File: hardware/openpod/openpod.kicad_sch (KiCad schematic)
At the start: 3 parts

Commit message: designed clickwheel and see if mpr121 can fit on it
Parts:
- ESP1: footprint openpod:ESP32-S3-WROOM-2 -> RF_Module:ESP32-S3-WROOM-2
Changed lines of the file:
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@@
       (effects (font (size 1.27 1.27)) (justify left))
     )
-    (property "Footprint" "openpod:ESP32-S3-WROOM-2" (at 148.082 201.422 0)
+    (property "Footprint" "RF_Module:ESP32-S3-WROOM-2" (at 148.082 201.422 0)
       (effects (font (size 1.27 1.27)) hide)
     )

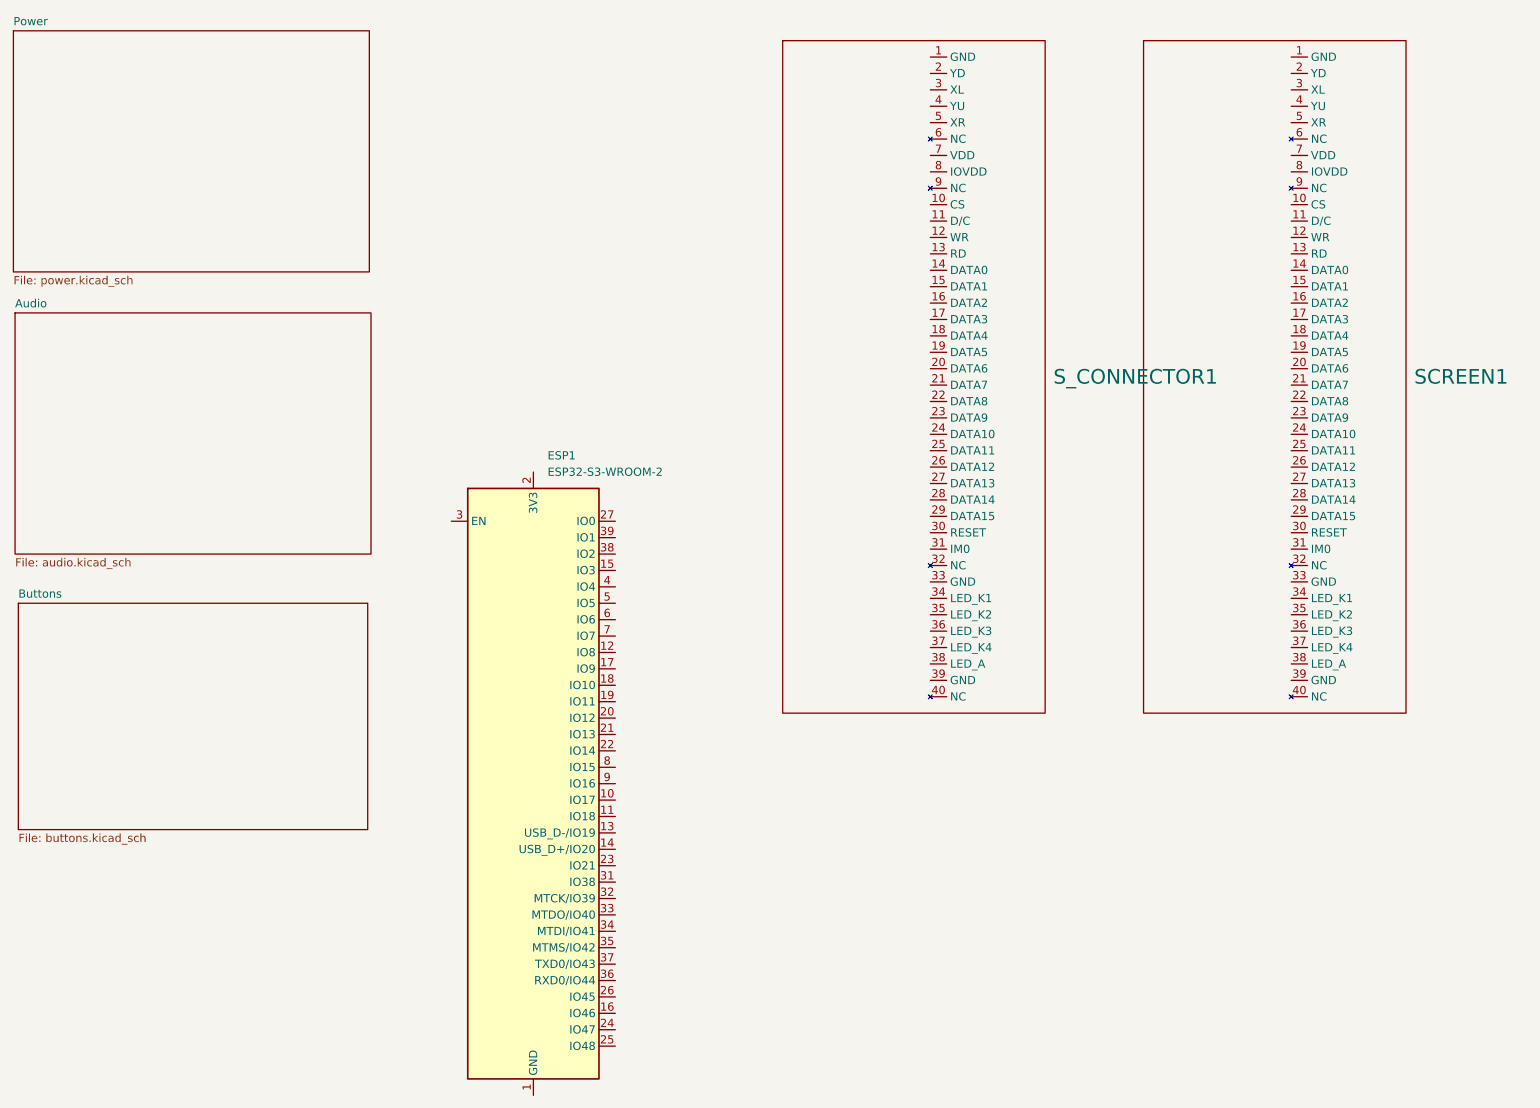
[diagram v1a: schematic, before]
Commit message: added bluetooth
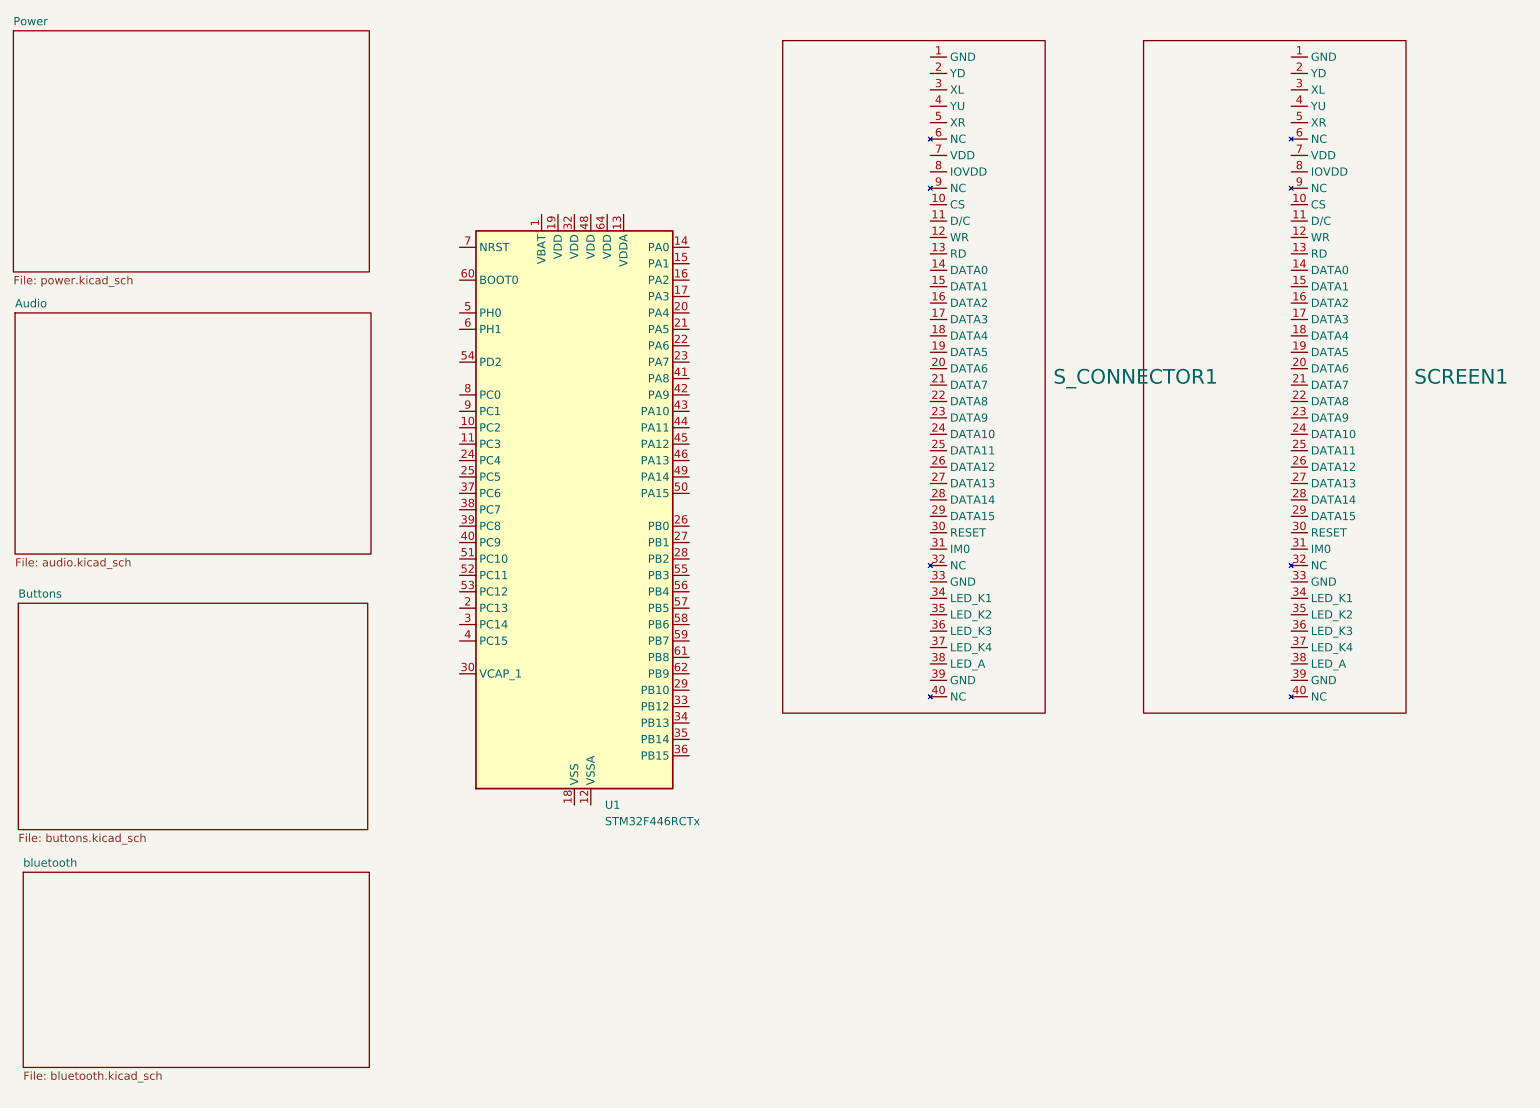
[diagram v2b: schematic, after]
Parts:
- removed ESP1: ESP32-S3-WROOM-2, RF_Module:ESP32-S3-WROOM-2, symbol RF_Module:ESP32-S3-WROOM-2
- added U1: STM32F446RCTx, Package_QFP:LQFP-64_10x10mm_P0.5mm, symbol MCU_ST_STM32F4:STM32F446RCTx
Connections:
- new net: U1.18 (VSS), U1.31 (VSS), U1.47 (VSS), U1.63 (VSS)
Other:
- added sheet bluetooth (bluetooth.kicad_sch)
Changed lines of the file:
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@@
 (kicad_sch (version 20230121) (generator eeschema)
   (paper "A4")
-  (symbol (lib_id "RF_Module:ESP32-S3-WROOM-2") (at 148.082 140.462 0) (unit 1)
+  (symbol (lib_id "MCU_ST_STM32F4:STM32F446RCTx") (at 154.432 98.044 0) (unit 1)
     (in_bom yes) (on_board yes) (dnp no) (fields_autoplaced)
-    (property "Reference" "ESP1" (at 150.2761 89.662 0)
+    (property "Reference" "U1" (at 159.1661 143.764 0)
       (effects (font (size 1.27 1.27)) (justify left))
     )
-    (property "Value" "ESP32-S3-WROOM-2" (at 150.2761 92.202 0)
+    (property "Value" "STM32F446RCTx" (at 159.1661 146.304 0)
       (effects (font (size 1.27 1.27)) (justify left))
     )
-    (property "Footprint" "RF_Module:ESP32-S3-WROOM-2" (at 148.082 201.422 0)
-      (effects (font (size 1.27 1.27)) hide)
-    )
-    (property "Datasheet" "https://www.espressif.com/sites/default/files/documentation/esp32-s3-wroom-2_datasheet_en.pdf" (at 148.082 203.962 0)
-      (effects (font (size 1.27 1.27)) hide)
-    )
-    (property "Manufacturer" "Espressif Systems" (at 148.082 140.462 0)
-      (effects (font (size 1.27 1.27)) hide)
-    )
-    (property "Part number" "ESP32-S3-WROOM-2-N32R16V" (at 148.082 140.462 0)
-      (effects (font (size 1.27 1.27)) hide)
-    )
-    (property "Supplier" "DigiKey" (at 148.082 140.462 0)
-      (effects (font (size 1.27 1.27)) hide)
-    )
-    (property "Supplier Part number" "1965-ESP32-S3-WROOM-2-N32R16VTR-ND" (at 148.082 140.462 0)
-      (effects (font (size 1.27 1.27)) hide)
-    )
+    (property "Footprint" "Package_QFP:LQFP-64_10x10mm_P0.5mm" (at 139.192 141.224 0)
+      (effects (font (size 1.27 1.27)) (justify right) hide)
+    )
+    (property "Datasheet" "https://www.st.com/resource/en/datasheet/stm32f446rc.pdf" (at 154.432 98.044 0)
+      (effects (font (size 1.27 1.27)) hide)
+    )
+    (property "Manufacturer" "STMicroelectronics" (at 154.432 98.044 0)
+      (effects (font (size 1.27 1.27)) hide)
+    )
+    (property "Part number" "STM32F446RCT6TR" (at 154.432 98.044 0)
+      (effects (font (size 1.27 1.27)) hide)
+    )
+    (property "Supplier" "DigiKey" (at 154.432 98.044 0)
+      (effects (font (size 1.27 1.27)) hide)
+    )
+    (property "Supplier Part number" "497-19357-2-ND" (at 154.432 98.044 0)
+      (effects (font (size 1.27 1.27)) hide)
+    )
+    (pin "54")
+    (pin "5")
+    (pin "47")
+    (pin "8")
+    (pin "42")
+    (pin "48")
+    (pin "56")
+    (pin "23")
+    (pin "9")
+    (pin "53")
+    (pin "31")
+    (pin "4")
+    (pin "49")
+    (pin "63")
+    (pin "16")
+    (pin "50")
+    (pin "29")
+    (pin "30")
+    (pin "46")
+    (pin "27")
+    (pin "26")
+    (pin "62")
+    (pin "24")
+    (pin "13")
+    (pin "64")
+    (pin "20")
+    (pin "34")
+    (pin "44")
+    (pin "41")
+    (pin "40")
+    (pin "51")
+    (pin "37")
+    (pin "25")
+    (pin "60")
+    (pin "55")
+    (pin "61")
+    (pin "6")
+    (pin "43")
+    (pin "45")
+    (pin "28")
+    (pin "3")
+    (pin "52")
+    (pin "7")
     (pin "39")
+    (pin "38")
+    (pin "33")
+    (pin "36")
     (pin "17")
-    (pin "40")
-    (pin "4")
-    (pin "31")
-    (pin "41")
-    (pin "8")
+    (pin "21")
+    (pin "32")
+    (pin "19")
+    (pin "58")
+    (pin "11")
+    (pin "35")
+    (pin "2")
+    (pin "22")
+    (pin "18")
+    (pin "57")
+    (pin "59")
+    (pin "12")
+    (pin "14")
     (pin "15")
-    (pin "14")
     (pin "10")
-    (pin "11")
-    (pin "21")
-    (pin "20")
-    (pin "18")
-    (pin "36")
-    (pin "33")
-    (pin "35")
-    (pin "13")
-    (pin "3")
-    (pin "6")
-    (pin "27")
-    (pin "29")
-    (pin "25")
-    (pin "28")
-    (pin "26")
-    (pin "23")
-    (pin "24")
-    (pin "22")
-    (pin "9")
-    (pin "19")
-    (pin "34")
-    (pin "2")
-    (pin "38")
-    (pin "5")
     (pin "1")
-    (pin "12")
-    (pin "16")
-    (pin "30")
-    (pin "32")
-    (pin "7")
-    (pin "37")
     (instances
       (project "openpod"
         (path "/0122bb8c-dbef-4db1-a6c6-9be780a38d9f"
-          (reference "ESP1") (unit 1)
+          (reference "U1") (unit 1)
         )
       )
@@
       )
     )
+  )
+  (sheet (at 69.088 154.178) (size 53.594 30.226) (fields_autoplaced)
+    (stroke (width 0.1524) (type solid))
+    (fill (color 0 0 0 0.0000))
+    (property "Sheetname" "bluetooth" (at 69.088 153.4664 0)
+      (effects (font (size 1.27 1.27)) (justify left bottom))
+    )
+    (property "Sheetfile" "bluetooth.kicad_sch" (at 69.088 184.9886 0)
+      (effects (font (size 1.27 1.27)) (justify left top))
+    )
+    (instances
+      (project "openpod"
+        (path "/0122bb8c-dbef-4db1-a6c6-9be780a38d9f" (page "5"))
+      )
+    )
